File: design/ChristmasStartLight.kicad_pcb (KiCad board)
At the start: 2 copper layers, 12.5 x 25.8 mm, 8 parts, among them P101 CONN_01X02, Q101 MMBT3904-7-F, SW101 MHSS1104, U101 ICM7555CBAZ-T

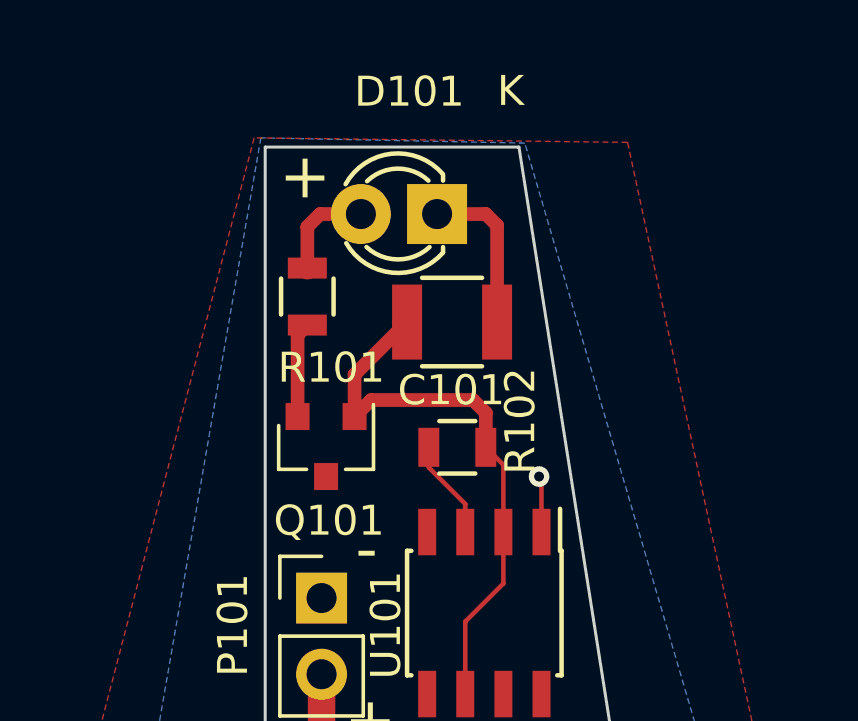
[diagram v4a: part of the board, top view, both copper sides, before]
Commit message: Finished v3 fixes including layout and submitted to OshPark
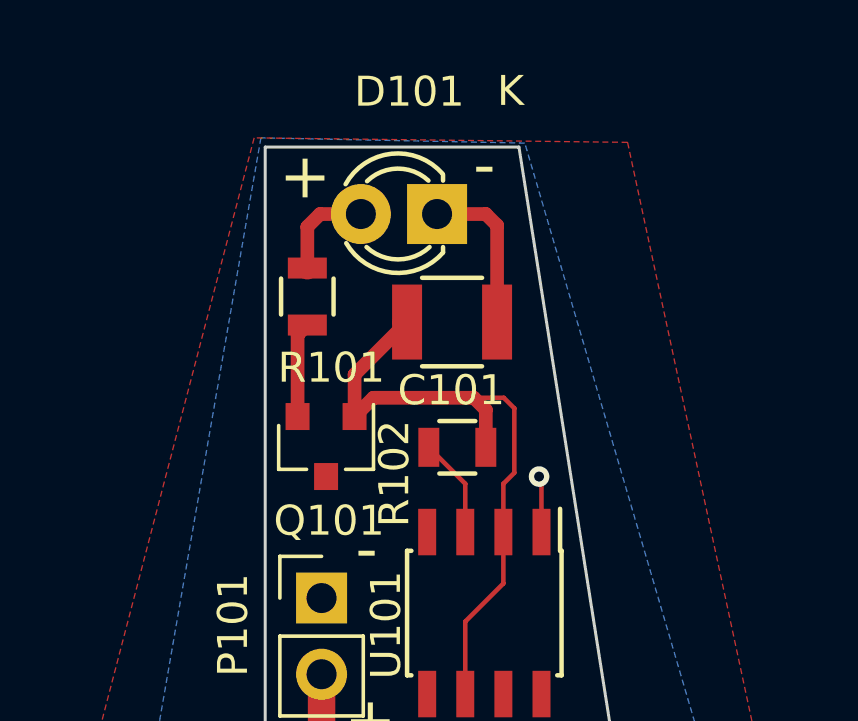
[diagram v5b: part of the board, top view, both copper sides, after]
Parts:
- R101: value 220 -> 3.1k
- turned R102 to 0 degrees
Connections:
- R102 pad 1: Net-(C101-Pad1) -> Net-(R102-Pad1)
- R102 pad 2: Net-(R102-Pad2) -> Net-(C101-Pad1)
- U101 pad 3: Net-(R102-Pad2) -> Net-(R102-Pad1)
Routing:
- net Net-(R102-Pad1): track 0.00 -> 3.33 mm
- net Net-(R102-Pad2): track 3.33 -> 0.00 mm
- net Net-(C101-Pad1): track 19.4 -> 22.2 mm
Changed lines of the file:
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@@
     (links 17)
     (no_connects 0)
-    (area 113.170219 49.9226 271.710714 194.375)
+    (area 123.520999 52.642299 136.150001 78.550001)
     (thickness 1.6)
-    (drawings 13)
-    (tracks 32)
+    (drawings 14)
+    (tracks 34)
     (zones 0)
     (modules 8)
@@
   (net 4 +9V)
   (net 5 /VCC)
-  (net 6 "Net-(R102-Pad2)")
-  (net 7 "Net-(SW101-Pad2)")
-  (net 8 "Net-(Q101-Pad2)")
+  (net 6 "Net-(SW101-Pad2)")
+  (net 7 "Net-(Q101-Pad2)")
+  (net 8 "Net-(R102-Pad1)")
   (net_class Default "This is the default net class."
     (clearance 0.1524)
@@
     (add_net "Net-(D101-Pad2)")
     (add_net "Net-(Q101-Pad2)")
-    (add_net "Net-(R102-Pad2)")
+    (add_net "Net-(R102-Pad1)")
     (add_net "Net-(SW101-Pad2)")
   )
@@
       (net 2 "Net-(C101-Pad1)"))
     (pad 2 smd rect (at -1 0.95 270) (size 0.9 0.8) (layers F.Cu F.Paste F.Mask)
-      (net 8 "Net-(Q101-Pad2)"))
+      (net 7 "Net-(Q101-Pad2)"))
     (pad 3 smd rect (at 1 0 270) (size 0.9 0.8) (layers F.Cu F.Paste F.Mask)
       (net 5 /VCC))
@@
       (effects (font (size 1 1) (thickness 0.15)))
     )
-    (fp_text value 220 (at -2.675 -0.575 180) (layer F.Fab) hide
+    (fp_text value 3.1k (at -2.675 -0.575 180) (layer F.Fab) hide
       (effects (font (size 1 1) (thickness 0.15)))
     )
@@
     (fp_line (start -0.6 -0.875) (end 0.6 -0.875) (layer F.SilkS) (width 0.15))
     (pad 1 smd rect (at -0.95 0 90) (size 0.7 1.3) (layers F.Cu F.Paste F.Mask)
-      (net 8 "Net-(Q101-Pad2)"))
+      (net 7 "Net-(Q101-Pad2)"))
     (pad 2 smd rect (at 0.95 0 90) (size 0.7 1.3) (layers F.Cu F.Paste F.Mask)
       (net 3 "Net-(D101-Pad2)"))
@@
   )
   (module Resistors_SMD:R_0805 (layer F.Cu)
-    (at 129.975 62.7 180)
+    (at 129.975 62.7)
     (descr "Resistor SMD 0805, reflow soldering, Vishay (see dcrcw.pdf)")
     (tags "resistor 0805")
     (attr smd)
-    (fp_text reference R102 (at -2.1 0.875 450) (layer F.SilkS)
-      (effects (font (size 1 1) (thickness 0.15)))
-    )
-    (fp_text value 300K (at 0 2.1 180) (layer F.Fab) hide
+    (fp_text reference R102 (at -2.1 0.875 270) (layer F.SilkS)
+      (effects (font (size 1 1) (thickness 0.15)))
+    )
+    (fp_text value 300K (at 0 2.1) (layer F.Fab) hide
       (effects (font (size 1 1) (thickness 0.15)))
     )
@@
     (fp_line (start 0.6 0.875) (end -0.6 0.875) (layer F.SilkS) (width 0.15))
     (fp_line (start -0.6 -0.875) (end 0.6 -0.875) (layer F.SilkS) (width 0.15))
-    (pad 1 smd rect (at -0.95 0 180) (size 0.7 1.3) (layers F.Cu F.Paste F.Mask)
+    (pad 1 smd rect (at -0.95 0) (size 0.7 1.3) (layers F.Cu F.Paste F.Mask)
+      (net 8 "Net-(R102-Pad1)"))
+    (pad 2 smd rect (at 0.95 0) (size 0.7 1.3) (layers F.Cu F.Paste F.Mask)
       (net 2 "Net-(C101-Pad1)"))
-    (pad 2 smd rect (at 0.95 0 180) (size 0.7 1.3) (layers F.Cu F.Paste F.Mask)
-      (net 6 "Net-(R102-Pad2)"))
     (model Resistors_SMD.3dshapes/R_0805.wrl
       (at (xyz 0 0 0))
@@
       (net 5 /VCC) (clearance 0.127))
     (pad 2 thru_hole circle (at 2.5908 -1.6002) (size 1.27 1.27) (drill 0.7874) (layers *.Cu *.Mask F.SilkS)
-      (net 7 "Net-(SW101-Pad2)") (clearance 0.127))
+      (net 6 "Net-(SW101-Pad2)") (clearance 0.127))
     (pad 1 thru_hole circle (at -2.3876 1.6002) (size 1.27 1.27) (drill 0.7874) (layers *.Cu *.Mask F.SilkS)
       (net 4 +9V) (clearance 0.127))
@@
       (net 5 /VCC) (clearance 0.127))
     (pad 2 thru_hole circle (at 2.5908 1.6002) (size 1.27 1.27) (drill 0.7874) (layers *.Cu *.Mask F.SilkS)
-      (net 7 "Net-(SW101-Pad2)") (clearance 0.127))
+      (net 6 "Net-(SW101-Pad2)") (clearance 0.127))
   )
   (module bth-ic-footprint:SOIC-8_3.9x4.9mm_Pitch1.27mm (layer F.Cu)
@@
       (net 2 "Net-(C101-Pad1)"))
     (pad 3 smd rect (at -2.7 0.635 270) (size 1.55 0.6) (layers F.Cu F.Paste F.Mask)
-      (net 6 "Net-(R102-Pad2)"))
+      (net 8 "Net-(R102-Pad1)"))
     (pad 4 smd rect (at -2.7 1.905 270) (size 1.55 0.6) (layers F.Cu F.Paste F.Mask)
       (net 5 /VCC))
@@
     )
   )
+  (gr_text - (at 130.875 53.3) (layer F.SilkS)
+    (effects (font (size 1.5 1.5) (thickness 0.3)))
+  )
   (gr_text 1.9.2017 (at 211.575 193.025) (layer Dwgs.User)
     (effects (font (size 1.5 1.5) (thickness 0.3)))
@@
     (effects (font (size 0.992 0.992) (thickness 0.1972)) (justify mirror))
   )
+  (segment (start 131.3 58.525) (end 131.3 55.3) (width 0.4572) (layer F.Cu) (net 1))
+  (segment (start 131.3 55.3) (end 130.925 54.925) (width 0.4572) (layer F.Cu) (net 1))
+  (segment (start 130.925 54.925) (end 129.3 54.925) (width 0.4572) (layer F.Cu) (net 1))
   (segment (start 132.78 65.525) (end 132.78 63.755) (width 0.1524) (layer F.Cu) (net 1))
   (via (at 132.7 63.675) (size 0.6858) (drill 0.3302) (layers F.Cu B.Cu) (net 1))
   (segment (start 132.78 63.755) (end 132.7 63.675) (width 0.1524) (layer F.Cu) (net 1))
-  (segment (start 131.3 58.525) (end 131.3 55.3) (width 0.4572) (layer F.Cu) (net 1))
-  (segment (start 130.925 54.925) (end 129.3 54.925) (width 0.4572) (layer F.Cu) (net 1))
-  (segment (start 131.3 55.3) (end 130.925 54.925) (width 0.4572) (layer F.Cu) (net 1))
+  (segment (start 131.51 65.525) (end 131.51 63.915) (width 0.1524) (layer F.Cu) (net 2))
+  (segment (start 131.525 61.05) (end 130.525 61.05) (width 0.1524) (layer F.Cu) (net 2))
+  (segment (start 131.875 61.4) (end 131.525 61.05) (width 0.1524) (layer F.Cu) (net 2))
+  (segment (start 131.875 63.55) (end 131.875 61.4) (width 0.1524) (layer F.Cu) (net 2))
+  (segment (start 131.51 63.915) (end 131.875 63.55) (width 0.1524) (layer F.Cu) (net 2))
+  (segment (start 130.925 62.7) (end 130.925 61.45) (width 0.4572) (layer F.Cu) (net 2))
+  (segment (start 130.925 61.45) (end 130.525 61.05) (width 0.4572) (layer F.Cu) (net 2))
+  (segment (start 127.175 61.05) (end 126.55 61.675) (width 0.4572) (layer F.Cu) (net 2))
+  (segment (start 130.525 61.05) (end 127.175 61.05) (width 0.4572) (layer F.Cu) (net 2))
   (segment (start 126.55 61.675) (end 126.55 60.275) (width 0.4572) (layer F.Cu) (net 2))
   (segment (start 126.55 60.275) (end 128.3 58.525) (width 0.4572) (layer F.Cu) (net 2))
-  (segment (start 130.925 62.7) (end 130.925 61.55) (width 0.4572) (layer F.Cu) (net 2))
-  (segment (start 127.1 61.125) (end 126.55 61.675) (width 0.4572) (layer F.Cu) (net 2))
-  (segment (start 130.5 61.125) (end 127.1 61.125) (width 0.4572) (layer F.Cu) (net 2))
-  (segment (start 130.925 61.55) (end 130.5 61.125) (width 0.4572) (layer F.Cu) (net 2))
   (segment (start 130.24 70.925) (end 130.24 68.51) (width 0.1524) (layer F.Cu) (net 2))
   (segment (start 131.51 67.24) (end 131.51 65.525) (width 0.1524) (layer F.Cu) (net 2))
@@
   (segment (start 128.025 58.525) (end 128.3 58.525) (width 0.4572) (layer F.Cu) (net 2))
   (segment (start 128 58.525) (end 128.3 58.525) (width 0.1524) (layer F.Cu) (net 2))
-  (segment (start 131.51 65.525) (end 131.51 63.285) (width 0.1524) (layer F.Cu) (net 2))
-  (segment (start 131.51 63.285) (end 130.925 62.7) (width 0.1524) (layer F.Cu) (net 2))
   (segment (start 124.975 56.725) (end 124.975 55.35) (width 0.4572) (layer F.Cu) (net 3))
   (segment (start 125.4 54.925) (end 126.76 54.925) (width 0.4572) (layer F.Cu) (net 3))
@@
   (segment (start 125.45 70.265) (end 125.45 73.4624) (width 0.9144) (layer F.Cu) (net 4))
   (segment (start 125.45 73.4624) (end 126.2124 74.2248) (width 0.9144) (layer F.Cu) (net 4))
-  (segment (start 130.24 65.525) (end 130.24 64.59) (width 0.1524) (layer F.Cu) (net 6))
-  (segment (start 129.025 63.375) (end 129.025 62.7) (width 0.1524) (layer F.Cu) (net 6))
-  (segment (start 130.24 64.59) (end 129.025 63.375) (width 0.1524) (layer F.Cu) (net 6))
-  (segment (start 131.1908 77.4252) (end 131.1908 74.2248) (width 0.9144) (layer B.Cu) (net 7))
-  (segment (start 124.65 61.675) (end 124.65 58.95) (width 0.4572) (layer F.Cu) (net 8))
-  (segment (start 124.65 58.95) (end 124.975 58.625) (width 0.4572) (layer F.Cu) (net 8))
+  (segment (start 131.1908 77.4252) (end 131.1908 74.2248) (width 0.9144) (layer B.Cu) (net 6))
+  (segment (start 124.65 61.675) (end 124.65 58.95) (width 0.4572) (layer F.Cu) (net 7))
+  (segment (start 124.65 58.95) (end 124.975 58.625) (width 0.4572) (layer F.Cu) (net 7))
+  (segment (start 130.24 65.525) (end 130.24 63.915) (width 0.1524) (layer F.Cu) (net 8))
+  (segment (start 130.24 63.915) (end 129.025 62.7) (width 0.1524) (layer F.Cu) (net 8))
   (zone (net 5) (net_name /VCC) (layer F.Cu) (hatch edge 0.508)
     (connect_pads (clearance 0.254))

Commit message: Misc changes
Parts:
- moved C101 71.4 mm to (64.8, 28.9)
- moved D101 71.4 mm to (64.3, 25.2)
- moved R102 71.4 mm to (65.0, 33.0)
- moved SW101 71.4 mm to (63.6, 46.1)
- moved P101 71.4 mm to (60.5, 38.0)
- moved Q101 71.4 mm to (60.6, 33.0)
- moved R101 71.4 mm to (60.0, 28.0)
- moved U101 71.4 mm to (65.9, 38.5)
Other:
- board text removed: "1.9.2017"
- board text removed: "v2"
